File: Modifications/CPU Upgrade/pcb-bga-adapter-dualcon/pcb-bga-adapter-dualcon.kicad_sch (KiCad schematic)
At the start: 3 parts, among them J1 54722-0604, J2 55560-0607

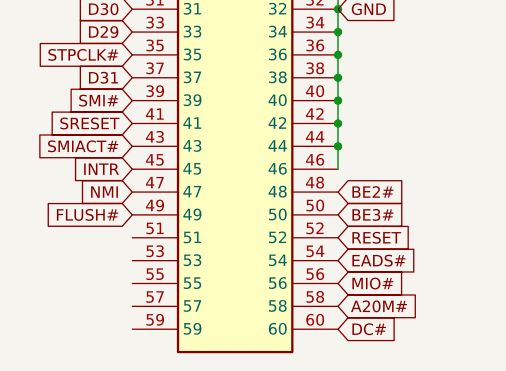
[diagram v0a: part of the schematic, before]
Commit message: Updated CPU Board
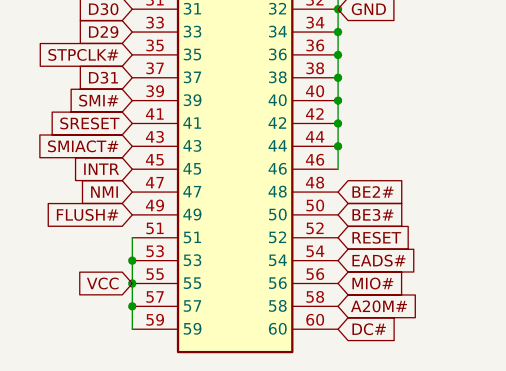
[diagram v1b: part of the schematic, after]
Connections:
- net VCC: now also J2.51, J2.53, J2.55, J2.57, J2.59
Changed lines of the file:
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@@
 	)
 	(junction
+		(at 29.21 179.07)
+		(diameter 0)
+		(color 0 0 0 0)
+	)
+	(junction
 		(at 186.69 163.83)
 		(diameter 0)
@@
 	)
 	(junction
+		(at 29.21 184.15)
+		(diameter 0)
+		(color 0 0 0 0)
+	)
+	(junction
 		(at 140.97 163.83)
 		(diameter 0)
@@
 	)
 	(junction
+		(at 29.21 181.61)
+		(diameter 0)
+		(color 0 0 0 0)
+	)
+	(junction
 		(at 173.99 17.78)
 		(diameter 0)
@@
 	(wire
 		(pts
+			(xy 29.21 184.15) (xy 29.21 186.69)
+		)
+		(stroke
+			(width 0)
+			(type default)
+		)
+	)
+	(wire
+		(pts
 			(xy 245.11 17.78) (xy 247.65 17.78)
 		)
@@
 	(wire
 		(pts
+			(xy 29.21 181.61) (xy 29.21 184.15)
+		)
+		(stroke
+			(width 0)
+			(type default)
+		)
+	)
+	(wire
+		(pts
 			(xy 204.47 17.78) (xy 207.01 17.78)
 		)
@@
 	(wire
 		(pts
+			(xy 29.21 176.53) (xy 29.21 179.07)
+		)
+		(stroke
+			(width 0)
+			(type default)
+		)
+	)
+	(wire
+		(pts
 			(xy 29.21 85.09) (xy 29.21 87.63)
 		)
@@
 	(wire
 		(pts
+			(xy 29.21 179.07) (xy 29.21 181.61)
+		)
+		(stroke
+			(width 0)
+			(type default)
+		)
+	)
+	(wire
+		(pts
 			(xy 199.39 163.83) (xy 201.93 163.83)
 		)
@@
 			(effects
 				(font
+					(size 1.27 1.27)
+				)
+				(justify right)
+				(hide yes)
+			)
+		)
+	)
+	(global_label "VCC"
+		(shape input)
+		(at 29.21 181.61 180)
+		(fields_autoplaced yes)
+		(effects
+			(font
+				(size 1.27 1.27)
+			)
+			(justify right)
+		)
+		(property "Intersheetrefs" "${INTERSHEET_REFS}"
+			(at 22.5962 181.61 0)
+			(effects
+				(font
